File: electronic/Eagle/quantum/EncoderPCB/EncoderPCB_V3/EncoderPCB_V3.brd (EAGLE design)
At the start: 136 x 28 mm, 31 parts, among them IC1 STM32F031K6T6, IC2 STM32F031K6T6

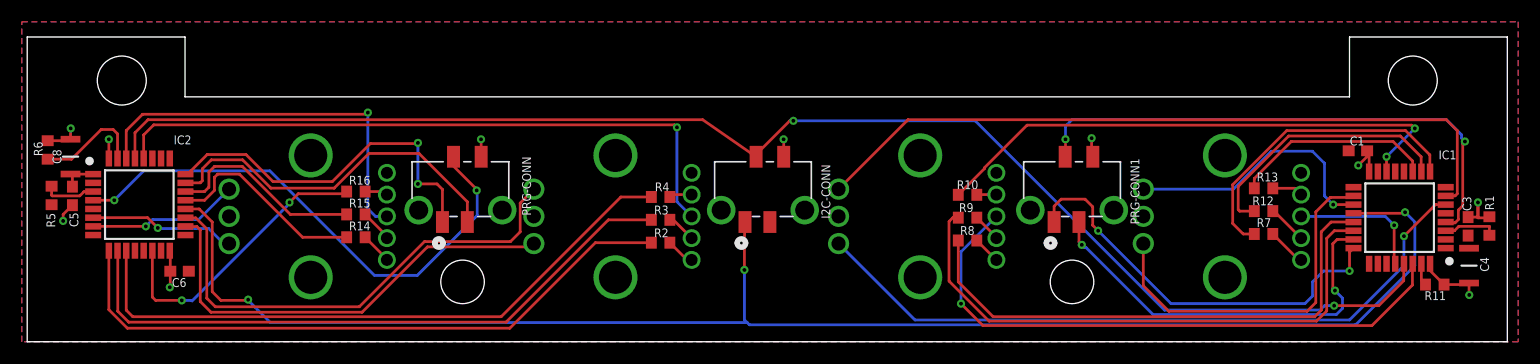
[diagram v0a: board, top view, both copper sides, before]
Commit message: implemented DMA UART Recive Display. Updates on Display side optic!
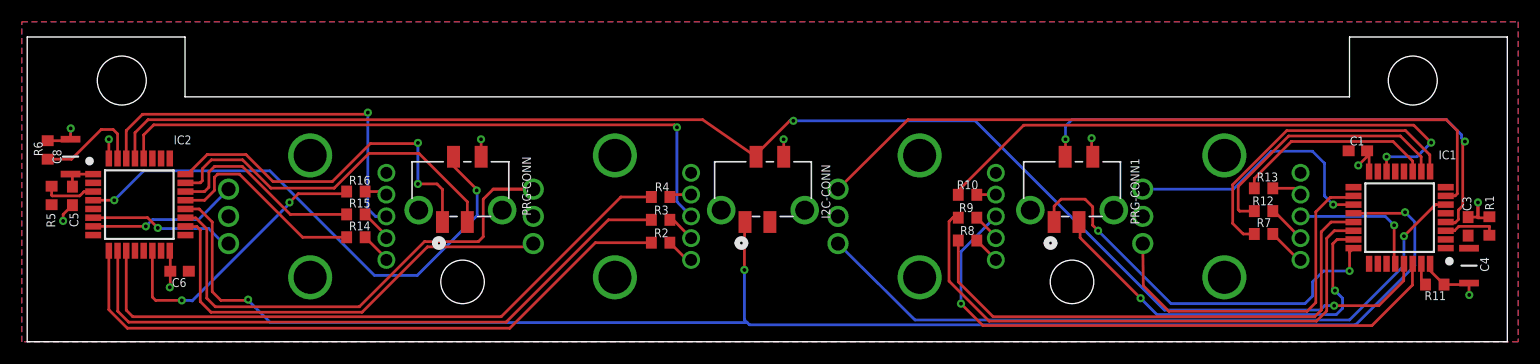
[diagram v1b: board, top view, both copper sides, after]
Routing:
- net A_B_ENC2: track 49.8 -> 53.2 mm

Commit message: started Plugin "klanghabitat connector"
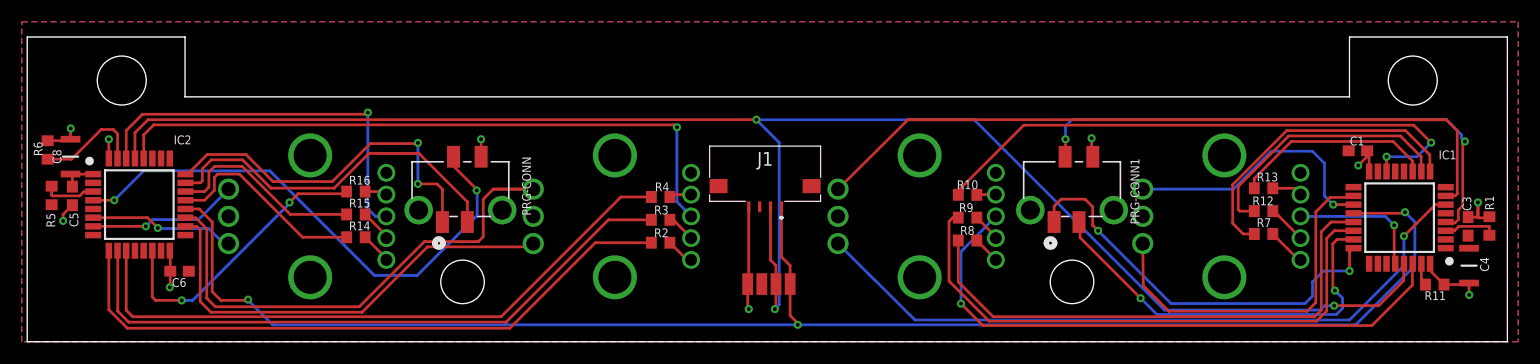
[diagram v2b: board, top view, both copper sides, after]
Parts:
- removed I2C-CONN: 90814-0204, electro_mechanical:MOLEX_90814-0204
- added J1: 686104183422, electro_mechanical:686104183422
- added U$1, U$2, U$3, U$4: TP, C_Sager_Bibliothek:OVAL_PAD
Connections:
- net +3V3: now also J1.3, U$3.P$1; no longer I2C-CONN.3
- net GND: now also J1.4, U$4.P$1; no longer I2C-CONN.4
- net I2C1_SCL: now also J1.2, U$2.P$1; no longer I2C-CONN.2
- net I2C1_SDA: now also J1.1, U$1.P$1; no longer I2C-CONN.1
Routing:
- net I2C1_SCL: track 131.8 -> 157.4 mm, vias 2 -> 3
- net GND: track 29.4 -> 37.3 mm
- net I2C1_SDA: track 142.9 -> 145.0 mm
